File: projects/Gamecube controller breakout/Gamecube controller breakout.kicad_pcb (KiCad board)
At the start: 2 copper layers, 8 parts

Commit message: 5v radio
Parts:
- added G***: LOGO, LOGO, F.Cu at (138.8, 91.2)

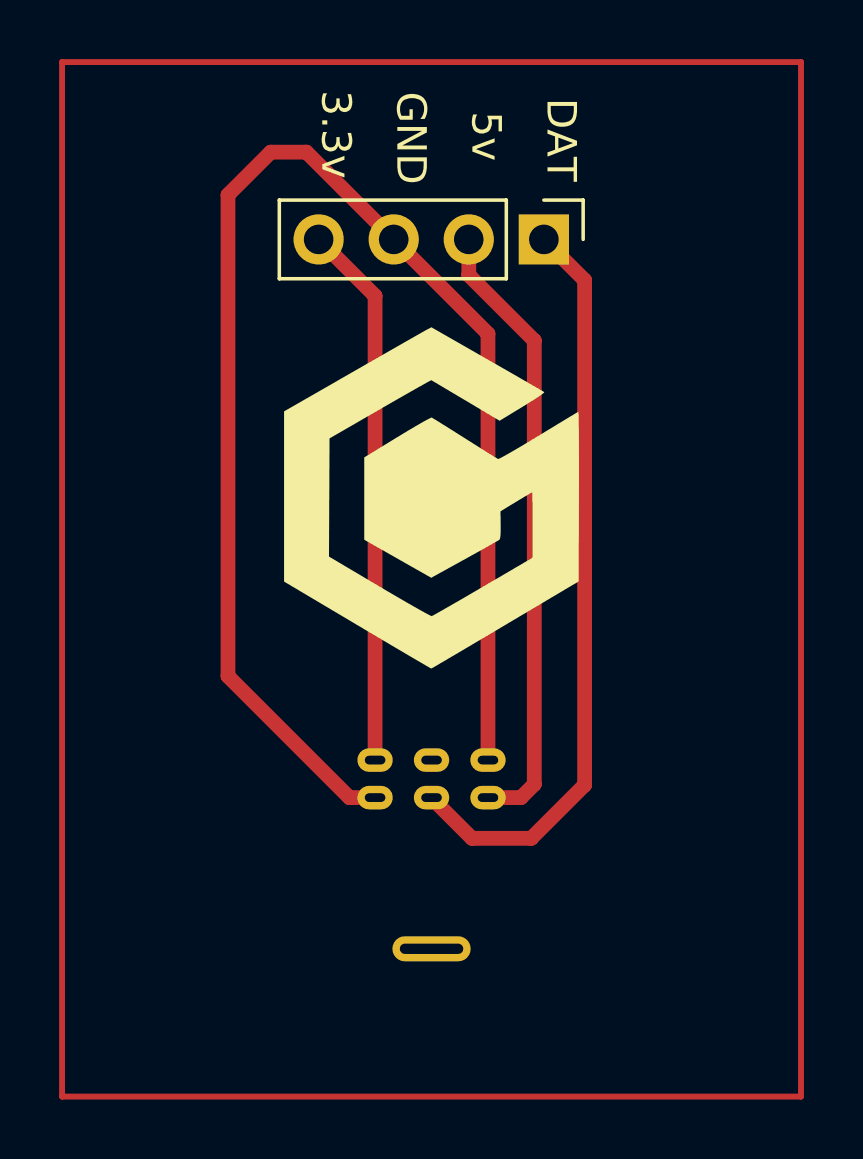
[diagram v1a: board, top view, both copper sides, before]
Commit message: thicc trace
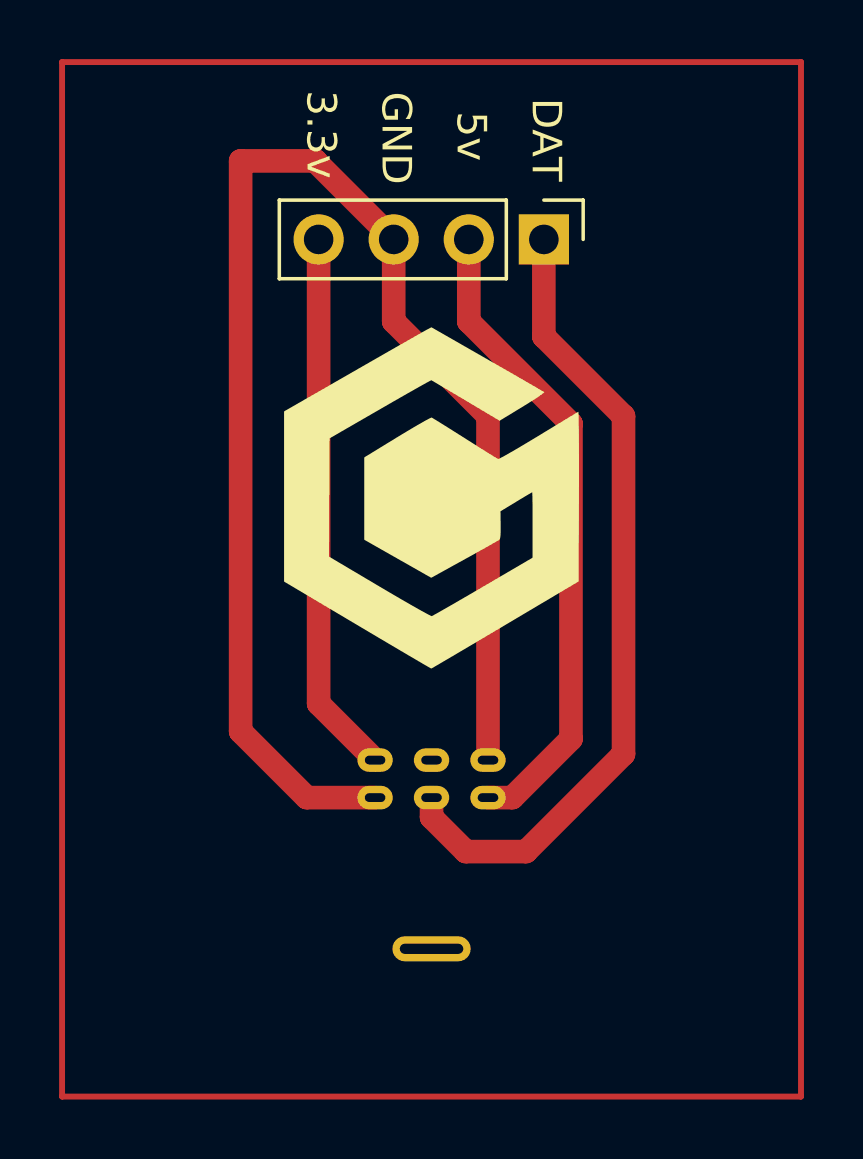
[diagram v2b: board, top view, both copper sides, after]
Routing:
- net (no net): track 114.4 -> 117.9 mm
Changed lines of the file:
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@@
 	)
 	(gr_text "5v"
-		(at 140.0526 78.078867 -90)
+		(at 139.5526 78.078867 -90)
 		(layer "F.SilkS")
 		(effects
@@
 	)
 	(gr_text "3.3v"
-		(at 134.9726 77.364581 -90)
+		(at 134.4726 77.364581 -90)
 		(layer "F.SilkS")
 		(effects
@@
 	)
 	(gr_text "DAT"
-		(at 142.5926 77.626486 -90)
+		(at 142.0926 77.626486 -90)
 		(layer "F.SilkS")
 		(effects
@@
 	)
 	(gr_text "GND"
-		(at 137.5126 77.4122 -90)
-		(layer "F.SilkS")
-		(effects
-			(font
-				(size 1 1)
-				(thickness 0.1)
-			)
-			(justify left bottom)
-		)
-	)
-	(segment
-		(start 136.8826 84.3222)
-		(end 134.9726 82.4122)
-		(width 0.5)
-		(layer "F.Cu")
-		(net 0)
-	)
-	(segment
-		(start 131.90604 80.90716)
-		(end 133.35384 79.45936)
-		(width 0.5)
-		(layer "F.Cu")
-		(net 0)
-	)
-	(segment
-		(start 143.97104 83.79064)
-		(end 142.5926 82.4122)
-		(width 0.5)
-		(layer "F.Cu")
-		(net 0)
-	)
-	(segment
-		(start 140.7026 85.6022)
-		(end 137.5126 82.4122)
-		(width 0.5)
-		(layer "F.Cu")
-		(net 0)
-	)
-	(segment
-		(start 140.7026 100.02758)
-		(end 140.7026 85.6022)
-		(width 0.5)
-		(layer "F.Cu")
-		(net 0)
-	)
-	(segment
-		(start 131.90604 97.18856)
-		(end 131.90604 80.90716)
-		(width 0.5)
-		(layer "F.Cu")
-		(net 0)
-	)
-	(segment
-		(start 138.7926 101.30652)
-		(end 140.16104 102.67496)
-		(width 0.5)
-		(layer "F.Cu")
-		(net 0)
-	)
-	(segment
-		(start 140.16104 102.67496)
-		(end 142.16764 102.67496)
-		(width 0.5)
-		(layer "F.Cu")
-		(net 0)
-	)
-	(segment
-		(start 133.35384 79.45936)
-		(end 134.55976 79.45936)
-		(width 0.5)
-		(layer "F.Cu")
-		(net 0)
-	)
-	(segment
-		(start 136.8826 101.29758)
-		(end 136.01506 101.29758)
-		(width 0.5)
-		(layer "F.Cu")
-		(net 0)
-	)
-	(segment
-		(start 143.97104 100.87156)
-		(end 143.97104 83.79064)
-		(width 0.5)
-		(layer "F.Cu")
-		(net 0)
-	)
-	(segment
-		(start 136.8826 100.02758)
-		(end 136.8826 84.3222)
-		(width 0.5)
+		(at 137.0126 77.4122 -90)
+		(layer "F.SilkS")
+		(effects
+			(font
+				(size 1 1)
+				(thickness 0.1)
+			)
+			(justify left bottom)
+		)
+	)
+	(segment
+		(start 145.288 88.392)
+		(end 145.288 99.822)
+		(width 0.8)
+		(layer "F.Cu")
+		(net 0)
+	)
+	(segment
+		(start 143.51 88.646)
+		(end 140.0526 85.1886)
+		(width 0.8)
 		(layer "F.Cu")
 		(net 0)
@@
 	(segment
 		(start 140.0526 82.4122)
-		(end 140.0526 83.61812)
-		(width 0.5)
-		(layer "F.Cu")
-		(net 0)
-	)
-	(segment
-		(start 142.26924 85.83476)
-		(end 142.26924 100.84616)
-		(width 0.5)
-		(layer "F.Cu")
-		(net 0)
-	)
-	(segment
-		(start 134.55976 79.45936)
-		(end 137.5126 82.4122)
-		(width 0.5)
-		(layer "F.Cu")
-		(net 0)
-	)
-	(segment
-		(start 142.26924 100.84616)
-		(end 141.81782 101.29758)
-		(width 0.5)
+		(end 140.0526 85.1886)
+		(width 0.8)
+		(layer "F.Cu")
+		(net 0)
+	)
+	(segment
+		(start 134.9726 98.11758)
+		(end 136.8826 100.02758)
+		(width 0.8)
+		(layer "F.Cu")
+		(net 0)
+	)
+	(segment
+		(start 139.954 103.124)
+		(end 138.7926 101.9626)
+		(width 0.8)
+		(layer "F.Cu")
+		(net 0)
+	)
+	(segment
+		(start 137.5126 82.4122)
+		(end 134.874 79.7736)
+		(width 0.8)
+		(layer "F.Cu")
+		(net 0)
+	)
+	(segment
+		(start 138.7926 101.9626)
+		(end 138.7926 101.29758)
+		(width 0.8)
+		(layer "F.Cu")
+		(net 0)
+	)
+	(segment
+		(start 140.7026 101.29758)
+		(end 141.52642 101.29758)
+		(width 0.8)
+		(layer "F.Cu")
+		(net 0)
+	)
+	(segment
+		(start 134.57158 101.29758)
+		(end 132.334 99.06)
+		(width 0.8)
+		(layer "F.Cu")
+		(net 0)
+	)
+	(segment
+		(start 142.5926 82.4122)
+		(end 142.5926 85.6966)
+		(width 0.8)
+		(layer "F.Cu")
+		(net 0)
+	)
+	(segment
+		(start 141.52642 101.29758)
+		(end 143.51 99.314)
+		(width 0.8)
+		(layer "F.Cu")
+		(net 0)
+	)
+	(segment
+		(start 140.7026 88.3786)
+		(end 137.5126 85.1886)
+		(width 0.8)
+		(layer "F.Cu")
+		(net 0)
+	)
+	(segment
+		(start 143.51 99.314)
+		(end 143.51 88.646)
+		(width 0.8)
+		(layer "F.Cu")
+		(net 0)
+	)
+	(segment
+		(start 142.5926 85.6966)
+		(end 145.288 88.392)
+		(width 0.8)
+		(layer "F.Cu")
+		(net 0)
+	)
+	(segment
+		(start 134.9726 82.4122)
+		(end 134.9726 98.11758)
+		(width 0.8)
+		(layer "F.Cu")
+		(net 0)
+	)
+	(segment
+		(start 132.334 79.756)
+		(end 132.334 99.06)
+		(width 0.8)
+		(layer "F.Cu")
+		(net 0)
+	)
+	(segment
+		(start 145.288 99.822)
+		(end 141.986 103.124)
+		(width 0.8)
+		(layer "F.Cu")
+		(net 0)
+	)
+	(segment
+		(start 141.986 103.124)
+		(end 139.954 103.124)
+		(width 0.8)
 		(layer "F.Cu")
 		(net 0)
@@
 	)
 	(segment
-		(start 142.16764 102.67496)
-		(end 143.97104 100.87156)
-		(width 0.5)
-		(layer "F.Cu")
-		(net 0)
-	)
-	(segment
-		(start 140.0526 83.61812)
-		(end 142.26924 85.83476)
-		(width 0.5)
-		(layer "F.Cu")
-		(net 0)
-	)
-	(segment
-		(start 136.01506 101.29758)
-		(end 131.90604 97.18856)
-		(width 0.5)
-		(layer "F.Cu")
-		(net 0)
-	)
-	(segment
-		(start 141.81782 101.29758)
-		(end 140.7026 101.29758)
-		(width 0.5)
+		(start 137.5126 85.1886)
+		(end 137.5126 82.4122)
+		(width 0.8)
+		(layer "F.Cu")
+		(net 0)
+	)
+	(segment
+		(start 136.8826 101.29758)
+		(end 134.57158 101.29758)
+		(width 0.8)
+		(layer "F.Cu")
+		(net 0)
+	)
+	(segment
+		(start 134.874 79.756)
+		(end 132.334 79.756)
+		(width 0.8)
+		(layer "F.Cu")
+		(net 0)
+	)
+	(segment
+		(start 134.874 79.7736)
+		(end 134.874 79.756)
+		(width 0.8)
+		(layer "F.Cu")
+		(net 0)
+	)
+	(segment
+		(start 140.7026 100.02758)
+		(end 140.7026 88.3786)
+		(width 0.8)
 		(layer "F.Cu")
 		(net 0)
@@
 		)
 	)
-	(group ""
-		(members "314daf2e-d1b2-4872-9a9e-49f75ec07c3b" "9caae731-cc8b-4ec2-a65a-e523822b3115"
-			"aa8d5ddd-01cf-46b7-9c6c-026f2e366ad7" "b2138e8c-001f-451a-8758-85e0041aefd4"
-			"d854463a-049e-4518-ac3d-a4d535fc8041"
-		)
-	)
